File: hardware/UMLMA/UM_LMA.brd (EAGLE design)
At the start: 18.9 x 16.8 mm, 10 parts, among them IC1 TINY13, J1 AVRISP6_TP

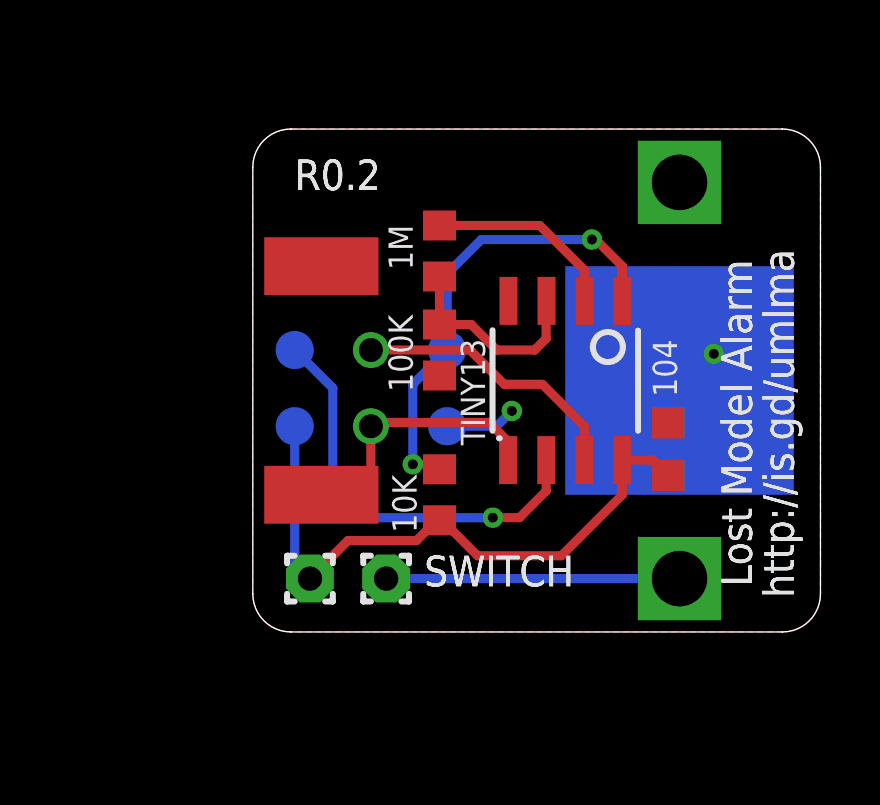
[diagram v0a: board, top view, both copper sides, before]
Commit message: Modified schematic and board to reflect hardware changes required for low voltage detection
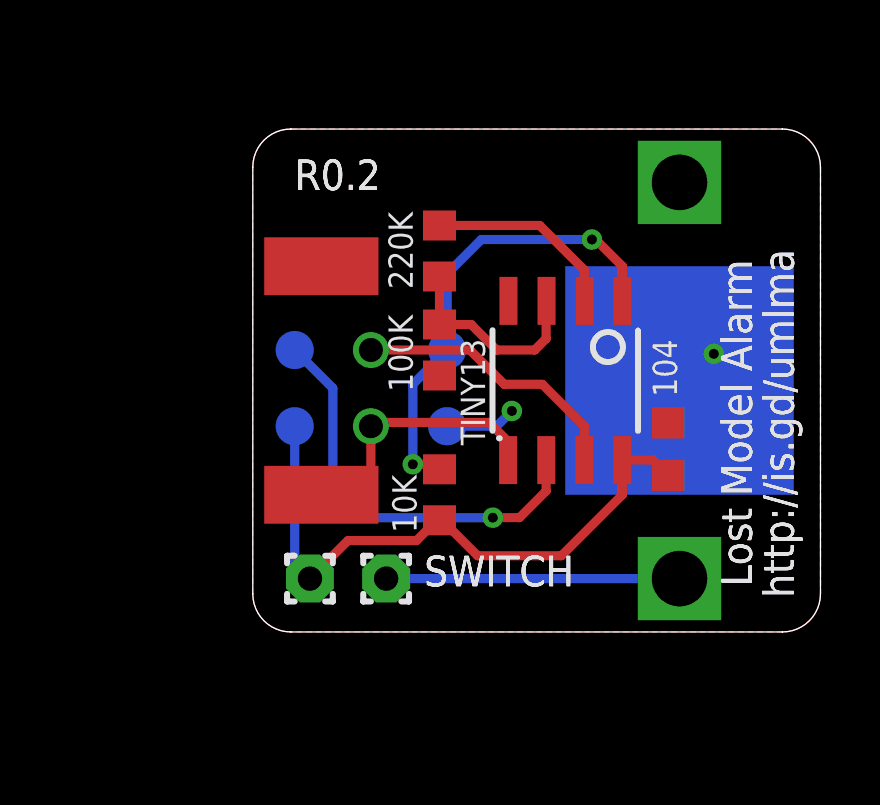
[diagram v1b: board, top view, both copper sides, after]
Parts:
- R3: value 1M -> 220K
- R4: value 100K -> 33K
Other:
- board text added: "220K"
- board text removed: "1M"
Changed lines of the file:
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@@
 <?xml version="1.0" encoding="utf-8"?>
 <!DOCTYPE eagle SYSTEM "eagle.dtd">
-<eagle version="6.4">
+<eagle version="7.1.0">
 <drawing>
 <settings>
@@
 <layer number="19" name="Unrouted" color="6" fill="1" visible="yes" active="yes"/>
 <layer number="20" name="Dimension" color="15" fill="1" visible="yes" active="yes"/>
-<layer number="21" name="tPlace" color="7" fill="1" visible="no" active="yes"/>
-<layer number="22" name="bPlace" color="7" fill="1" visible="no" active="yes"/>
-<layer number="23" name="tOrigins" color="15" fill="1" visible="no" active="yes"/>
-<layer number="24" name="bOrigins" color="15" fill="1" visible="no" active="yes"/>
-<layer number="25" name="tNames" color="7" fill="1" visible="no" active="yes"/>
-<layer number="26" name="bNames" color="7" fill="1" visible="no" active="yes"/>
-<layer number="27" name="tValues" color="7" fill="1" visible="no" active="yes"/>
-<layer number="28" name="bValues" color="7" fill="1" visible="no" active="yes"/>
+<layer number="21" name="tPlace" color="7" fill="1" visible="yes" active="yes"/>
+<layer number="22" name="bPlace" color="7" fill="1" visible="yes" active="yes"/>
+<layer number="23" name="tOrigins" color="15" fill="1" visible="yes" active="yes"/>
+<layer number="24" name="bOrigins" color="15" fill="1" visible="yes" active="yes"/>
+<layer number="25" name="tNames" color="7" fill="1" visible="yes" active="yes"/>
+<layer number="26" name="bNames" color="7" fill="1" visible="yes" active="yes"/>
+<layer number="27" name="tValues" color="7" fill="1" visible="yes" active="yes"/>
+<layer number="28" name="bValues" color="7" fill="1" visible="yes" active="yes"/>
 <layer number="29" name="tStop" color="7" fill="3" visible="yes" active="yes"/>
 <layer number="30" name="bStop" color="7" fill="6" visible="yes" active="yes"/>
@@
 <text x="7.744003125" y="6.223" size="0.8128" layer="121" font="vector" ratio="25" rot="R90">TINY13</text>
 <text x="5.461" y="3.302" size="0.8128" layer="121" font="vector" ratio="25" rot="R90">10K</text>
-<text x="5.334" y="12.065" size="0.8128" layer="121" font="vector" ratio="25" rot="R90">1M</text>
+<text x="5.334" y="11.43" size="0.8128" layer="121" font="vector" ratio="25" rot="R90">220K</text>
 <text x="5.334" y="8.001" size="0.8128" layer="121" font="vector" ratio="25" rot="R90">100K</text>
 <text x="12.192" y="15.113" size="1.016" layer="122" font="vector" ratio="20" rot="MR0">CR1225</text>
@@
 <pass name="Default">
 <param name="RoutingGrid" value="50mil"/>
+<param name="AutoGrid" value="1"/>
+<param name="Efforts" value="0"/>
+<param name="TopRouterVariant" value="1"/>
 <param name="tpViaShape" value="round"/>
 <param name="PrefDir.1" value="|"/>
@@
 <attribute name="BOM" value="EXCLUDE" x="4.445" y="1.778" size="1.778" layer="27" rot="R270" display="off"/>
 </element>
-<element name="R3" library="rcl" package="R0603" value="1M" x="6.223" y="12.7" smashed="yes" rot="R270">
+<element name="R3" library="rcl" package="R0603" value="220K" x="6.223" y="12.7" smashed="yes" rot="R270">
 <attribute name="PARTNO" value="ERJ-3GEYJ102V" x="6.223" y="12.7" size="1.778" layer="27" rot="R270" display="off"/>
-<attribute name="VALUE" x="5.334" y="12.065" size="0.8128" layer="27" rot="R90"/>
-</element>
-<element name="R4" library="rcl" package="R0603" value="100K" x="6.223" y="9.398" smashed="yes" rot="R270">
+<attribute name="VALUE" x="5.334" y="11.43" size="0.8128" layer="27" rot="R90"/>
+</element>
+<element name="R4" library="rcl" package="R0603" value="33K" x="6.223" y="9.398" smashed="yes" rot="R270">
 <attribute name="PARTNO" value="ERJ-3GEYJ102V" x="6.223" y="9.398" size="1.778" layer="27" rot="R270" display="off"/>
 <attribute name="VALUE" x="5.334" y="8.001" size="0.8128" layer="27" rot="R90"/>

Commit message: starting to convert to tiny25, config button, trying to re-do layout
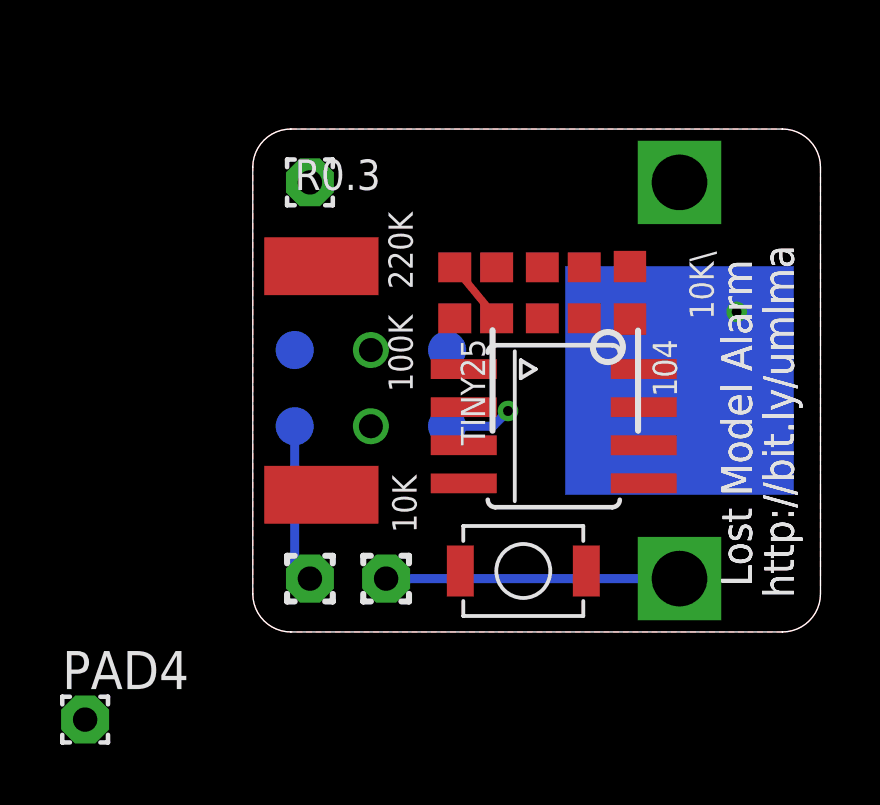
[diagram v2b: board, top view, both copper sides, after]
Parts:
- added PAD3: GND, wirepad:1,6/0,8
- added PAD4: VCC, wirepad:1,6/0,8
- added R2: 10K, rcl:R0603
- added S1: CONF, bt_electromech:3X4X2TACT
- IC1: value TINY13 -> TINY25; device atmel:8S1 -> bt_avr:SOIC8N
- moved R1 8.28 mm to (11.0, 11.3), turned to 270 degrees
- moved C1 5.36 mm to (12.6, 11.3)
- moved R4 2.69 mm to (8.13, 11.3), turned to 90 degrees
- moved IC1 1.57 mm to (10.0, 6.86), turned to 270 degrees
- moved R3 1.49 mm to (6.73, 11.3), turned to 90 degrees
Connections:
- net N$3 renamed VTEST
- net GND: now also PAD3.1, S1.P$1
- net SCK: now also R2.2, S1.P$2
- net VCC: now also PAD4.1, R2.1
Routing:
- net !RESET: track 16.2 -> 0.00 mm, vias 2 -> 0
- net VCC: track 20.7 -> 5.29 mm
- net MISO: track 14.2 -> 0.00 mm, vias 1 -> 0
- net SCK: track 9.30 -> 0.00 mm
- net MOSI: track 9.11 -> 0.00 mm
- net N$5: track 6.48 -> 0.00 mm
- net VTEST: track 6.93 -> 2.20 mm
- net GND: track 4.75 -> 6.07 mm
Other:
- board text added: "10K\"
- board text added: "R0.3"
- board text added: "TINY25"
- board text added: "http://bit.ly/umlma"
- board text removed: "R0.2"
- board text removed: "TINY13"
- board text removed: "http://is.gd/umlma"

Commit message: Revised PCB layout, reduced board length.
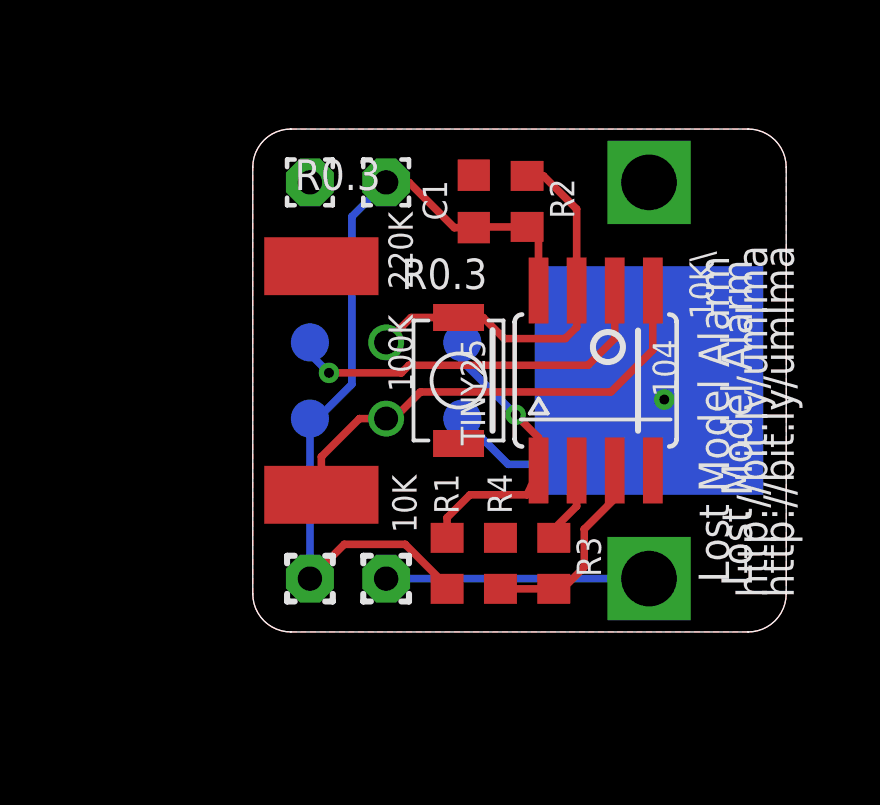
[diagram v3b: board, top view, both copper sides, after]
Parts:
- moved PAD4 20.5 mm to (4.45, 15.0)
- moved R1 10.1 mm to (6.48, 2.29), turned to 90 degrees
- moved R3 9.60 mm to (10.0, 2.29), turned to 270 degrees
- moved R4 9.02 mm to (8.26, 2.29)
- moved S1 6.71 mm to (6.86, 8.38), turned to 90 degrees
- moved C1 6.03 mm to (7.37, 14.4)
- moved R2 3.09 mm to (9.14, 14.4), turned to 90 degrees
- moved IC1 2.07 mm to (11.4, 8.38), turned to 0 degrees
- moved BAT 1.02 mm to (13.2, 8.38)
- moved J1 0.57 mm to (4.45, 8.38)
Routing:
- net VCC: track 5.29 -> 27.7 mm
- net MOSI: track 0.00 -> 15.8 mm
- net SCK: track 0.00 -> 13.2 mm
- net MISO: track 0.00 -> 12.9 mm, vias 0 -> 1
- net !RESET: track 0.00 -> 9.87 mm, vias 0 -> 1
- net VTEST: track 2.20 -> 6.74 mm
- net GND: track 6.07 -> 8.92 mm, vias 2 -> 1
- net N$5: track 0.00 -> 2.56 mm
- net N$2: track 9.78 -> 8.76 mm
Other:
- board size 18.9 x 16.8 mm -> 17.8 x 16.8 mm
